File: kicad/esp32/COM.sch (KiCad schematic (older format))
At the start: 1 part, among them P17 UART

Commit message: 自動配線成功
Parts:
- renumbered P17 to P16
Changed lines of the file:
@@
 $Descr A4 11693 8268
 encoding utf-8
-Sheet 12 13
+Sheet 12 14
 Title ""
 Date ""
@@
 $EndDescr
 $Comp
-L GND #PWR067
+L GND #PWR064
 U 1 1 57CDAC76
 P 4800 4200
-F 0 "#PWR067" H 4800 3950 50  0001 C CNN
+F 0 "#PWR064" H 4800 3950 50  0001 C CNN
 F 1 "GND" H 4800 4050 50  0000 C CNN
 F 2 "" H 4800 4200 50  0000 C CNN
@@
 	4800 3900 4700 3900
 $Comp
-L CONN_01X03 P17
+L CONN_01X03 P16
 U 1 1 57CDB029
 P 4500 4000
-F 0 "P17" H 4500 4250 50  0000 C CNN
+F 0 "P16" H 4500 4250 50  0000 C CNN
 F 1 "UART" V 4600 4000 50  0000 C CNN
 F 2 "Connectors_JST:JST_SH_BM03B-SRSS-TB_03x1.00mm_Straight" H 4500 4000 50  0001 C CNN

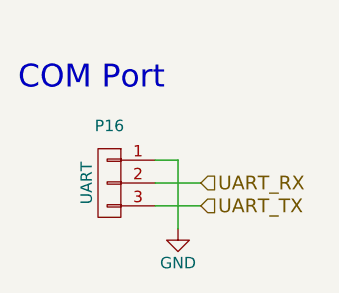
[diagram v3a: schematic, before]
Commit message: 2輪の基板を作成
部品を配置
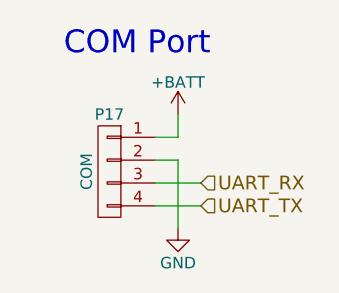
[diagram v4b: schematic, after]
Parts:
- removed P16: UART, Connectors_JST:JST_SH_BM03B-SRSS-TB_03x1.00mm_Straight, symbol CONN_01X03
- added P17: COM, Pin_Headers:Pin_Header_Straight_1x04_Pitch1.27mm, symbol CONN_01X04
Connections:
- net GND: now also P17.2 (P2)
- net UART_RX: now also P17.3 (P3)
- net UART_TX: now also P17.4 (P4)
- new net +BATT: P17.1 (P1)
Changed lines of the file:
@@
 $Descr A4 11693 8268
 encoding utf-8
-Sheet 12 14
+Sheet 9 13
 Title ""
 Date ""
@@
 $EndDescr
 $Comp
-L GND #PWR063
+L GND #PWR048
 U 1 1 57CDAC76
 P 4800 4200
-F 0 "#PWR063" H 4800 3950 50  0001 C CNN
+F 0 "#PWR048" H 4800 3950 50  0001 C CNN
 F 1 "GND" H 4800 4050 50  0000 C CNN
 F 2 "" H 4800 4200 50  0000 C CNN
@@
 Wire Wire Line
 	4800 3900 4700 3900
+Wire Wire Line
+	4900 4100 4700 4100
+Text Notes 4300 3450 0    100  ~ 0
+COM Port
 $Comp
-L CONN_01X03 P16
-U 1 1 57CDB029
-P 4500 4000
-F 0 "P16" H 4500 4250 50  0000 C CNN
-F 1 "UART" V 4600 4000 50  0000 C CNN
-F 2 "Connectors_JST:JST_SH_BM03B-SRSS-TB_03x1.00mm_Straight" H 4500 4000 50  0001 C CNN
-F 3 "" H 4500 4000 50  0000 C CNN
-	1    4500 4000
+L CONN_01X04 P17
+U 1 1 592C4BBD
+P 4500 3950
+F 0 "P17" H 4500 4200 50  0000 C CNN
+F 1 "COM" V 4600 3950 50  0000 C CNN
+F 2 "Pin_Headers:Pin_Header_Straight_1x04_Pitch1.27mm" H 4500 3950 50  0001 C CNN
+F 3 "" H 4500 3950 50  0000 C CNN
+	1    4500 3950
 	-1   0    0    -1
 $EndComp
+$Comp
+L +BATT #PWR049
+U 1 1 592C4BE4
+P 4800 3700
+F 0 "#PWR049" H 4800 3550 50  0001 C CNN
+F 1 "+BATT" H 4800 3840 50  0000 C CNN
+F 2 "" H 4800 3700 50  0000 C CNN
+F 3 "" H 4800 3700 50  0000 C CNN
+	1    4800 3700
+	1    0    0    -1
+$EndComp
 Wire Wire Line
-	4900 4100 4700 4100
-Text Notes 4100 3600 0    100  ~ 0
-COM Port
+	4800 3700 4800 3800
+Wire Wire Line
+	4800 3800 4700 3800
 $EndSCHEMATC
